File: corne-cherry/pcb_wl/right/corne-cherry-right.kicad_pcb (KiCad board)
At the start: 2 copper layers, 152.8 x 91.4 mm, 57 parts, among them J3 MJ-4PP-9, J4 OLED, J5 Conn_01x02_Female, SW22 SW_PUSH, SW23 SW_PUSH, SW24 SW_PUSH, SW25 SW_PUSH, SW26 SW_PUSH, SW27 SW_PUSH, SW28 SW_PUSH, SW29 SW_PUSH, SW30 SW_PUSH, SW31 SW_PUSH, SW32 SW_PUSH, SW33 SW_PUSH, SW34 SW_PUSH, SW35 SW_PUSH, SW36 SW_PUSH, SW37 SW_PUSH, SW38 SW_PUSH, SW39 SW_PUSH, SW40 SW_PUSH, SW41 SW_PUSH, SW42 SW_PUSH, SW43 SW_PUSH, SW44 SW_SPDT, U2 ProMicro

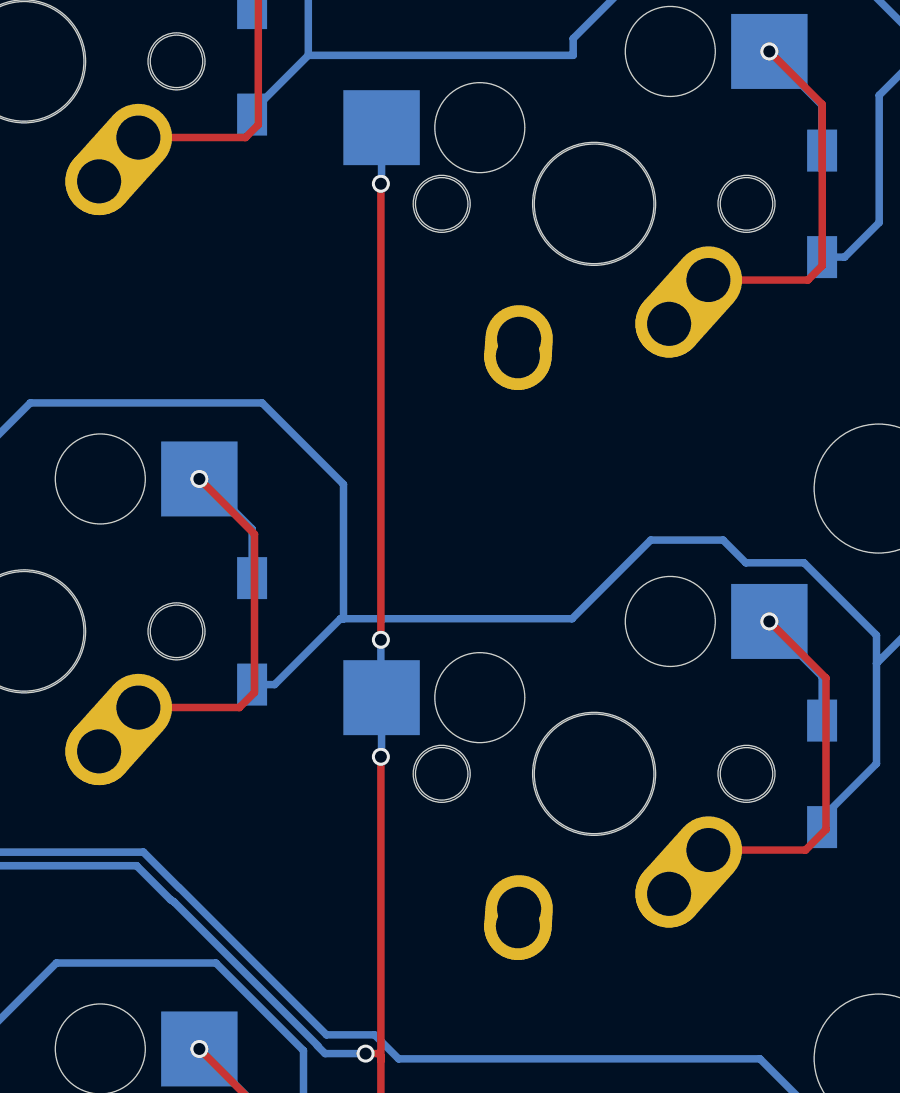
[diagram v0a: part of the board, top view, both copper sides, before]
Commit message: Two solder pads for 'p' and ';' were unrouted
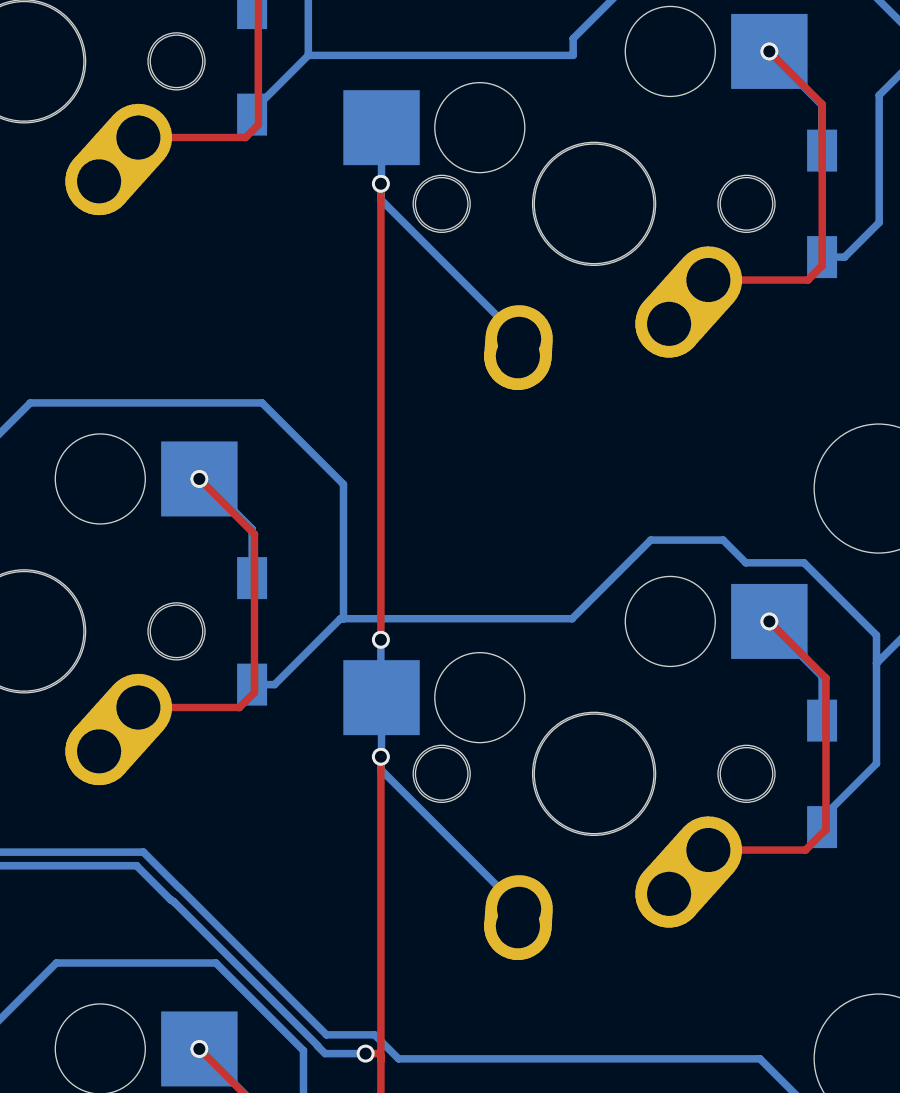
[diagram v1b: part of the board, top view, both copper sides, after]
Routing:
- net col1_r: track 159.6 -> 173.7 mm

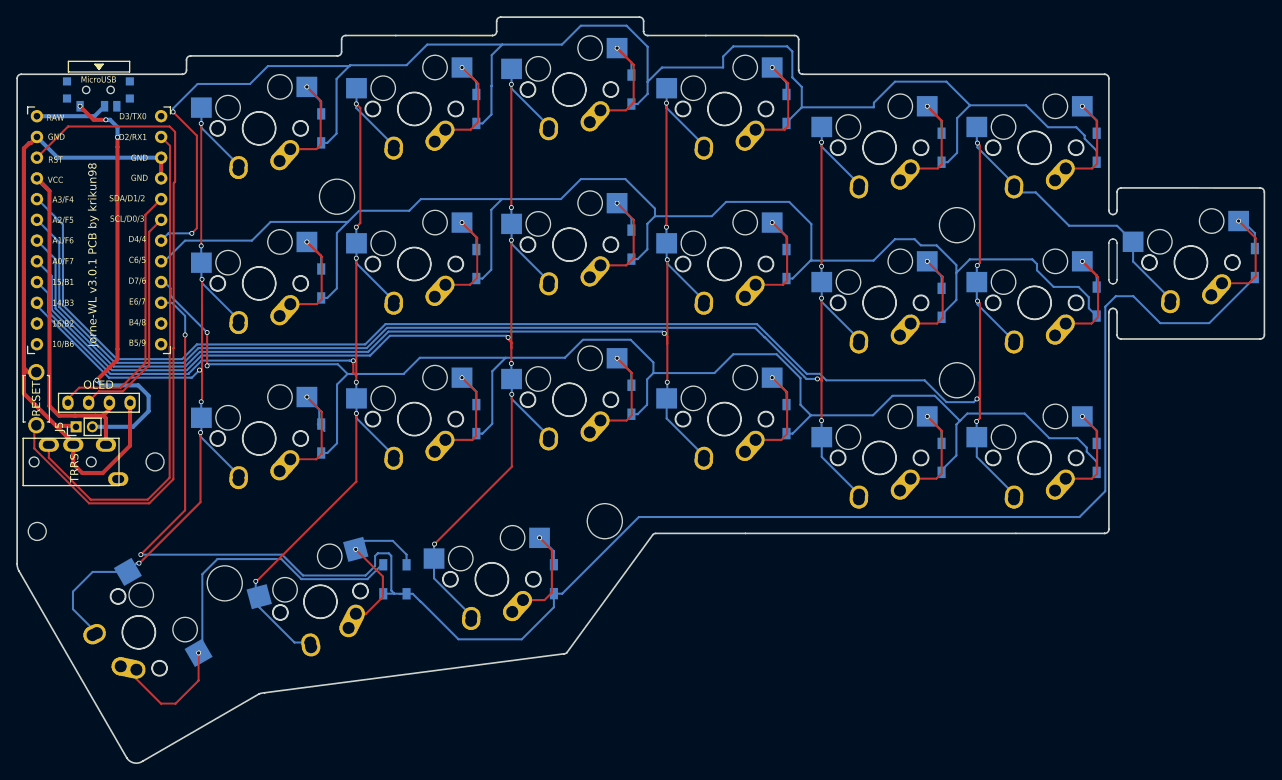
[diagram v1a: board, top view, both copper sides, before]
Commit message: Small revision bump: bigger battery header, smaller footprints
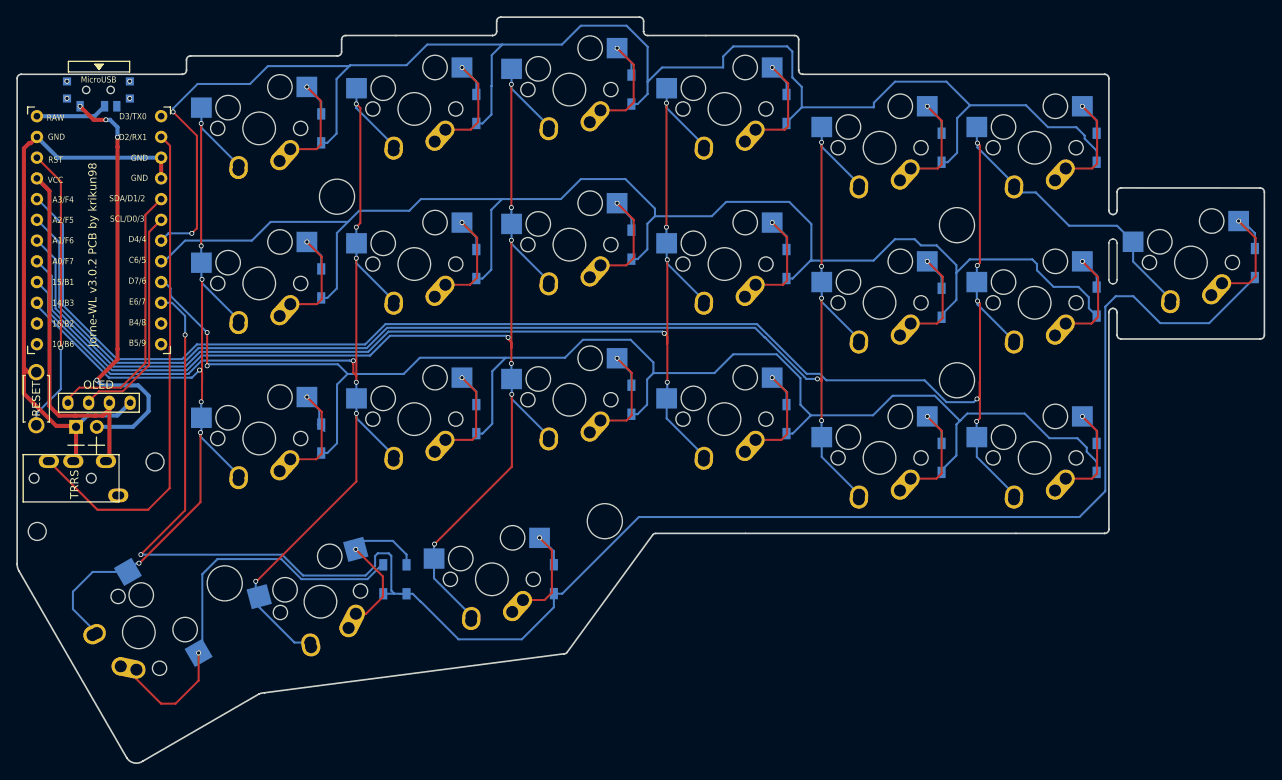
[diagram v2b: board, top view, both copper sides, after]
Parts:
- J5: footprint Connector_PinHeader_2.00mm:PinHeader_1x02_P2.00mm_Vertical -> kbd:Battery_Header
- moved J3 2.00 mm to (152.5, 76.3)
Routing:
- net reset_r: track 85.4 -> 35.6 mm, vias 0 -> 1
- net GNDA: track 80.6 -> 73.2 mm
- net VDD: track 43.1 -> 46.7 mm
- net data_r: track 62.9 -> 61.9 mm
- net (no net): vias 0 -> 4
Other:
- board text added: "Jorne-WL v3.0.2 PCB by krikun98"
- board text removed: "Jorne-WL v3.0.1 PCB by krikun98"
